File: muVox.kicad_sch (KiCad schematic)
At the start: 45 parts, among them J1 U/I INTERCONN., J10 IO1, J11 Alt.DC, J3 PROGRAMMER, J5 DC IN, J8 UFL, J9 IO0, SW1 EG120A, U1 XC6220B331MR, U3 ESP32-PICO-V3-02, U5 HT7463

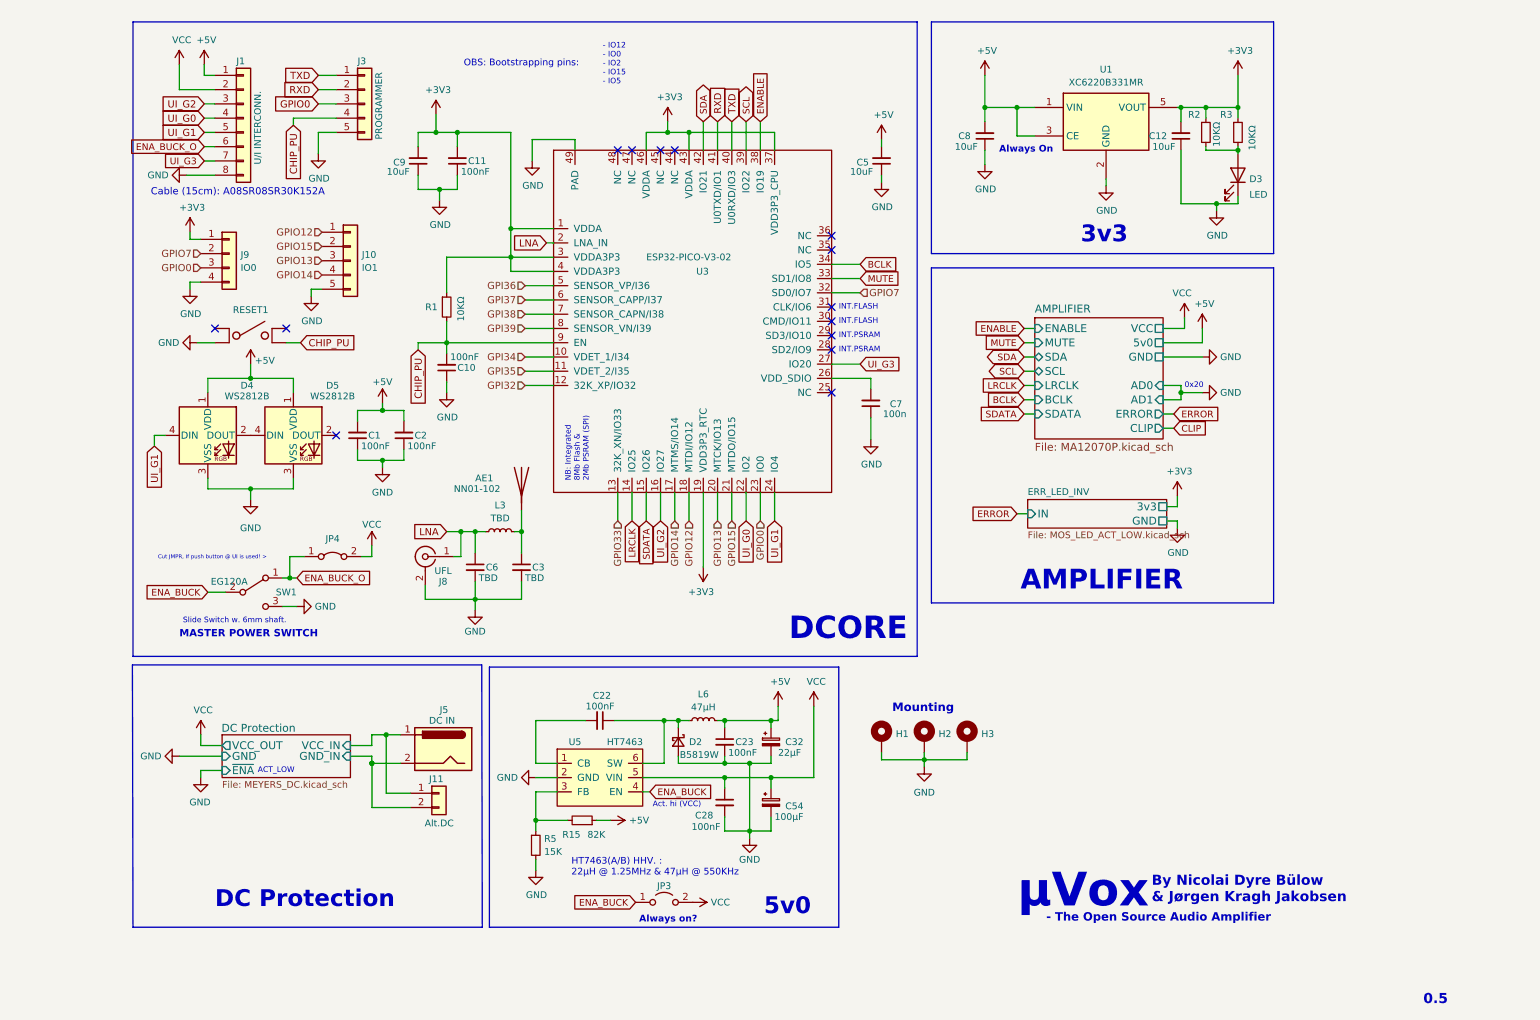
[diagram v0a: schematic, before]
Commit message: Latest revision - dc protection and change to wrover
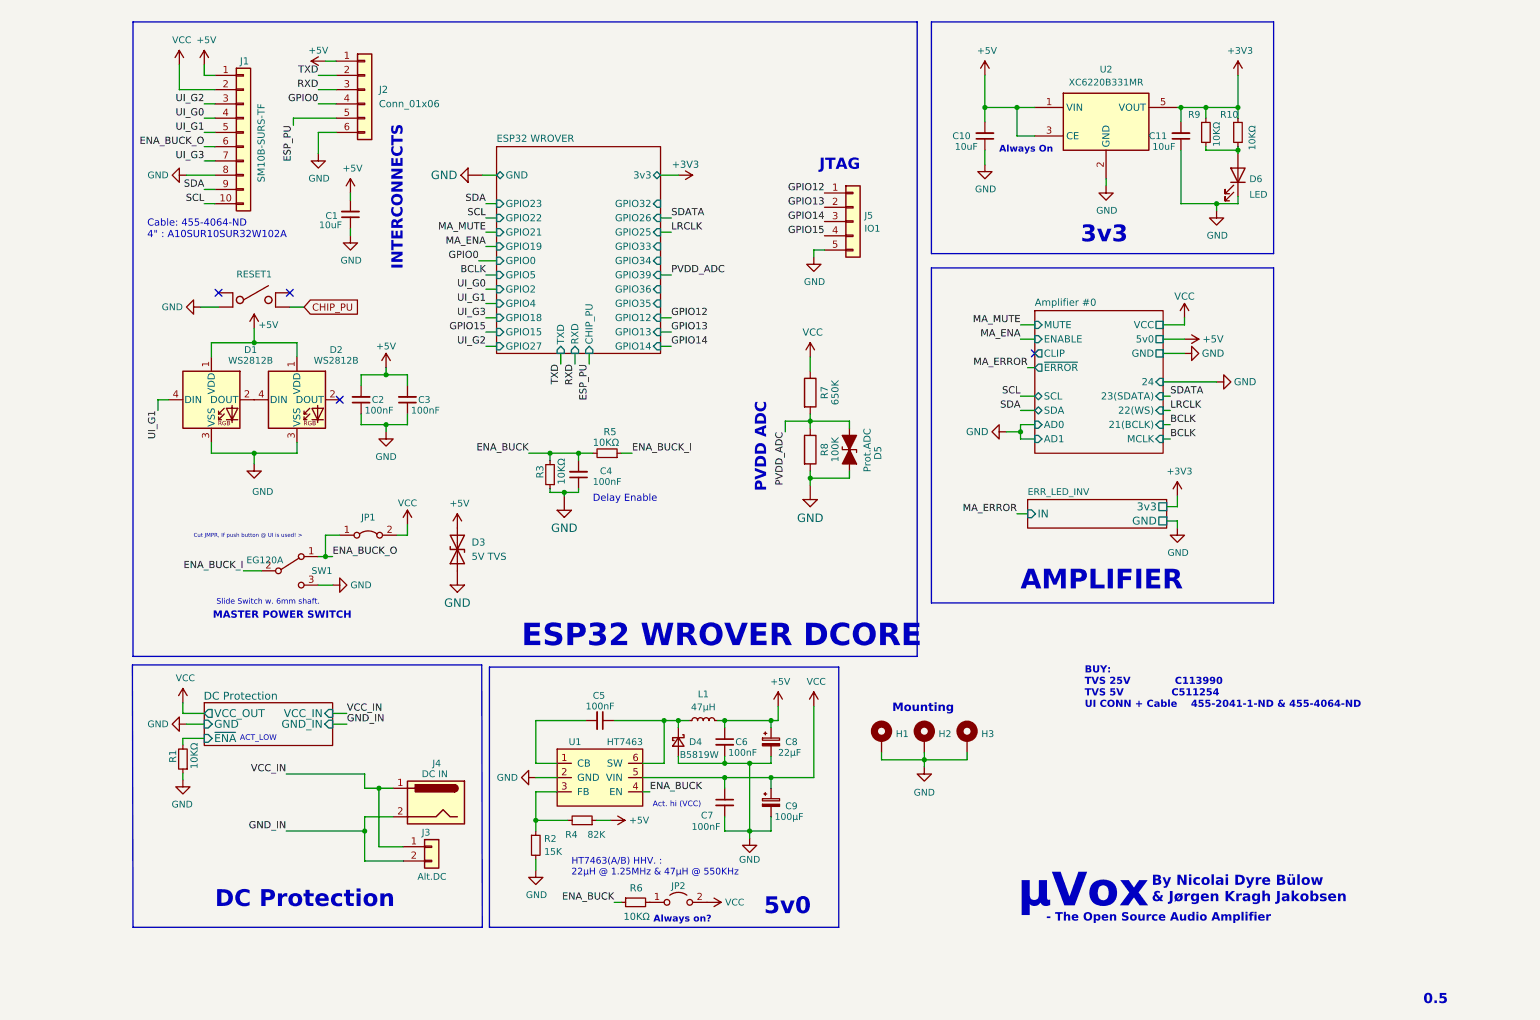
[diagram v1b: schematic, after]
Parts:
- removed AE1: NN01-102, Lib:XCVR_NN01-102, symbol Device:Antenna
- removed C10, C11: 100nF, Capacitor_SMD:C_0603_1608Metric, symbol Device:C_Small
- removed C3, C6: TBD, Capacitor_SMD:C_0402_1005Metric, symbol Device:C_Small
- removed C7: 100n, Capacitor_SMD:C_0603_1608Metric, symbol Device:C_Small
- removed C9: 10uF, Capacitor_SMD:C_0805_2012Metric, symbol Device:C_Small
- removed J1: U/I INTERCONN., Connector_JST:JST_SH_SM08B-SRSS-TB_1x08-1MP_P1.00mm_Horizontal, symbol Connector_Generic:Conn_01x08
- removed J3: PROGRAMMER, Connector_PinHeader_2.54mm:PinHeader_1x05_P2.54mm_Vertical, symbol Connector_Generic:Conn_01x05
- removed J8: UFL, Connector_Coaxial:U.FL_Hirose_U.FL-R-SMT-1_Vertical, symbol Connector:Conn_Coaxial
- removed J9: IO0, Connector_PinHeader_2.00mm:PinHeader_1x04_P2.00mm_Vertical, symbol Connector_Generic:Conn_01x04
- removed L3: TBD, Inductor_SMD:L_0402_1005Metric, symbol Device:L_Small
- removed U3: ESP32-PICO-V3-02, Package_DFN_QFN:QFN-48-1EP_7x7mm_P0.5mm_EP5.15x5.15mm_ThermalVias, symbol muVoxSyms:ESP32-PICO-V3-02
- added C4: 100nF, Capacitor_SMD:C_0603_1608Metric, symbol Device:C_Small
- added D3: 5V TVS, Diode_SMD:D_SOD-323, symbol Device:D_TVS
- added D5: Prot.ADC, Diode_SMD:D_SOD-323_HandSoldering, symbol Device:D_TVS_ALT
- added J1: SM10B-SURS-TF, Connector_JST:JST_SUR_SM10B-SURS-TF_1x10-1MP_P0.80mm_Horizontal, symbol Connector_Generic:Conn_01x10
- added J2: Conn_01x06, Connector_PinHeader_2.54mm:PinHeader_1x06_P2.54mm_Vertical, symbol Connector_Generic:Conn_01x06
- added R3, R5, R6: 10KΩ, Resistor_SMD:R_0603_1608Metric, symbol Device:R_Small
- added R7: 650K, Resistor_SMD:R_0603_1608Metric, symbol Device:R
- added R8: 100K, Resistor_SMD:R_0603_1608Metric, symbol Device:R
- renumbered C5 to C1, C8 to C10, C12 to C11, C1 to C2, C2 to C3, C22 to C5, C23 to C6, C28 to C7, C32 to C8, C54 to C9, D4 to D1, D5 to D2, D2 to D4, D3 to D6, J11 to J3, J5 to J4, J10 to J5, JP4 to JP1, JP3 to JP2, L6 to L1, R3 to R10, R5 to R2, R15 to R4, R2 to R9, U5 to U1, U1 to U2
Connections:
- net +3V3: no longer R1.1
- net +5V: now also D3.2 (A2), J1.1 (Pin_1), J2.1 (Pin_1)
- net CHIP_PU: no longer R1.2
- net ENA_BUCK: now also C4.2, R3.2, R5.2, R6.1; no longer JP2.1 (A), SW1.2 (B)
- net ENA_BUCK_O: now also J1.6 (Pin_6)
- net GND: now also R1.1, C4.1, D3.1 (A1), D5.2 (A2), J1.8 (Pin_8), J2.6 (Pin_6), R3.1, R8.2
- net GPIO0: now also J2.4 (Pin_4)
- net GPIO13: now also J5.2 (Pin_2); no longer J5.3 (Pin_3)
- net GPIO14: now also J5.3 (Pin_3); no longer J5.4 (Pin_4)
- net GPIO15: now also J5.4 (Pin_4); no longer J5.2 (Pin_2)
- net RXD: now also J2.3 (Pin_3)
- net SCL: now also J1.10 (Pin_10)
- net SDA: now also J1.9 (Pin_9)
- net TXD: now also J2.2 (Pin_2)
- net UI_G0: now also J1.4 (Pin_4)
- net UI_G1: now also J1.5 (Pin_5)
- net UI_G2: now also J1.3 (Pin_3)
- net UI_G3: now also J1.7 (Pin_7)
- net VCC: now also J1.2 (Pin_2), R7.1
- net DC Protection/GND_IN renamed GND_IN
- net DC Protection/VCC_IN renamed VCC_IN
- new net: JP2.1 (A), R6.2
- new net DC Protection/~{ENA}: R1.2
- new net ENA_BUCK_I: R5.1, SW1.2 (B)
- new net ESP_PU: J2.5 (Pin_5)
- new net PVDD_ADC: D5.1 (A1), R7.2, R8.1
- no-connect marks 14 -> 4
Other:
- removed sheet AMPLIFIER
- added sheet Amplifier #0 (ext_Sch/MA12070P.kicad_sch)
- added sheet ESP32 WROVER (ext_sch/ESP32WROVER.kicad_sch)
- note added: "BUY: TVS 25V C113990 TVS 5V C511254 UI CONN + Cable 455-2041-1-ND & 455-4064-ND"
- note added: "Cable: 455-4064-ND 4" : A10SUR10SUR32W102A"
- note added: "Delay Enable"
- note added: "ESP32 WROVER DCORE"
- note added: "INTERCONNECTS"
- note added: "JTAG"
- note added: "PVDD ADC"
- note removed: "- IO12 - IO0 - IO2 - IO15 - IO5"
- note removed: "0x20"
- note removed: "Cable (15cm): A08SR08SR30K152A"
- note removed: "DCORE"
- note removed: "INT.FLASH"
- note removed: "INT.PSRAM"
- note removed: "NB: Integrated 8Mb Flash & 2Mb PSRAM (SPI)"
- note removed: "OBS: Bootstrapping pins:"
- moved on the sheet: C1, C2, C3, D1, D2, J3, J4, J5, JP1, JP2, RESET1, SW1

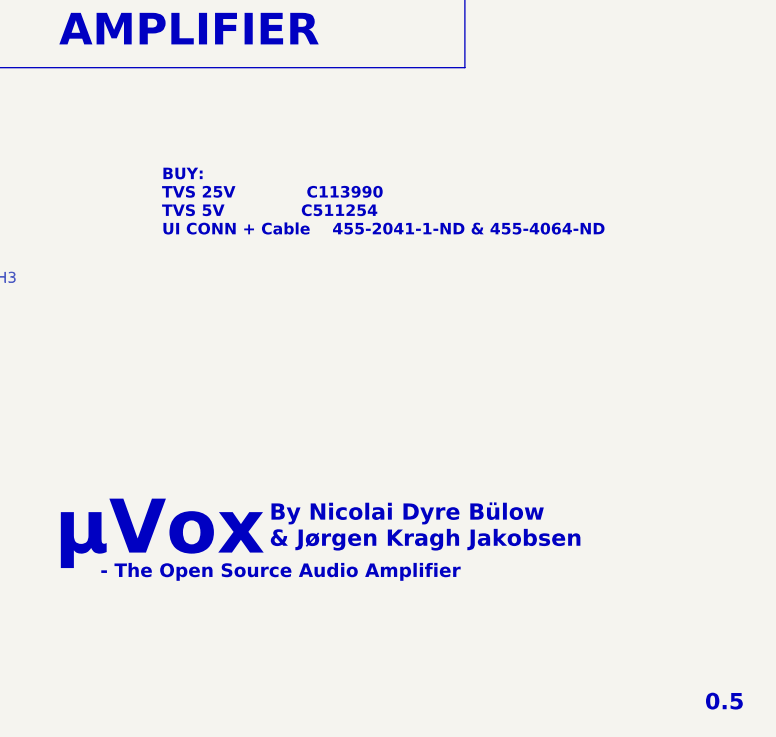
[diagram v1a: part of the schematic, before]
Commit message: Updated 3D-renders and readme
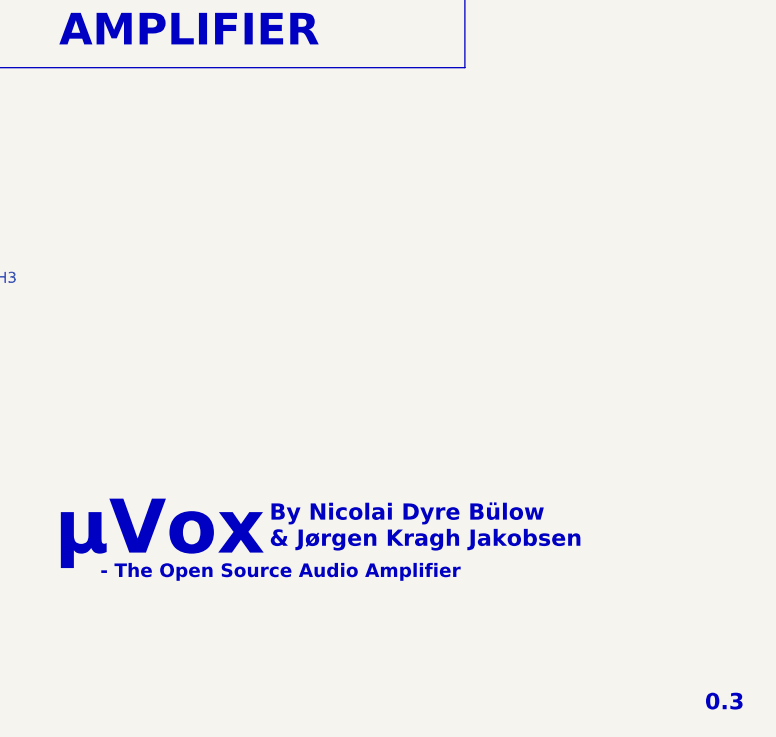
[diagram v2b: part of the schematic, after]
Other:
- note added: "0.3"
- note removed: "0.5"
- note removed: "BUY: TVS 25V C113990 TVS 5V C511254 UI CONN + Cable 455-2041-1-ND & 455-4064-ND"
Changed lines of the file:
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@@
     (effects (font (size 5.9944 5.9944) (thickness 1.1989) bold) (justify left bottom))
-  )
-  (text "BUY:\nTVS 25V 			C113990\nTVS 5V  			C511254\nUI CONN + Cable	455-2041-1-ND & 455-4064-ND\n"
-    (at 209.55 141.478 0)
-    (effects (font (size 1.27 1.27) bold) (justify left bottom))
   )
   (text "MASTER POWER SWITCH" (at 54.229 125.603 0)
@@
     (effects (font (size 0.9906 0.9906)) (justify left bottom))
   )
-  (text "0.5" (at 269.875 194.31 0)
+  (text "0.3\n" (at 269.875 194.31 0)
     (effects (font (size 1.8034 1.8034) (thickness 0.3607) bold) (justify left bottom))
   )
